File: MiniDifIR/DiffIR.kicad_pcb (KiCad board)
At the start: 2 copper layers, 33 x 24.8 mm, 17 parts, among them IC1 ATTINY25-SS, P1 AVR_ISP, P2 OUT

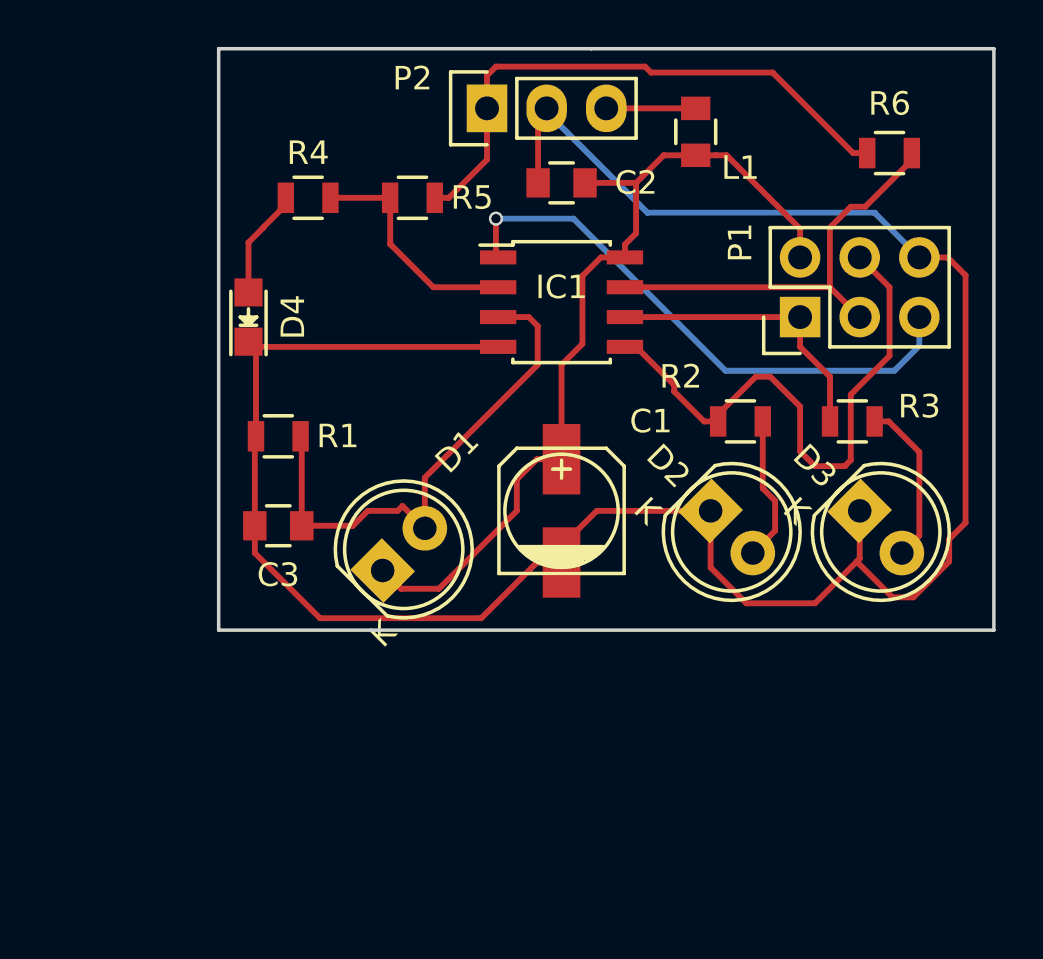
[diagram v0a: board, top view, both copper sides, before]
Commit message: thickened traces
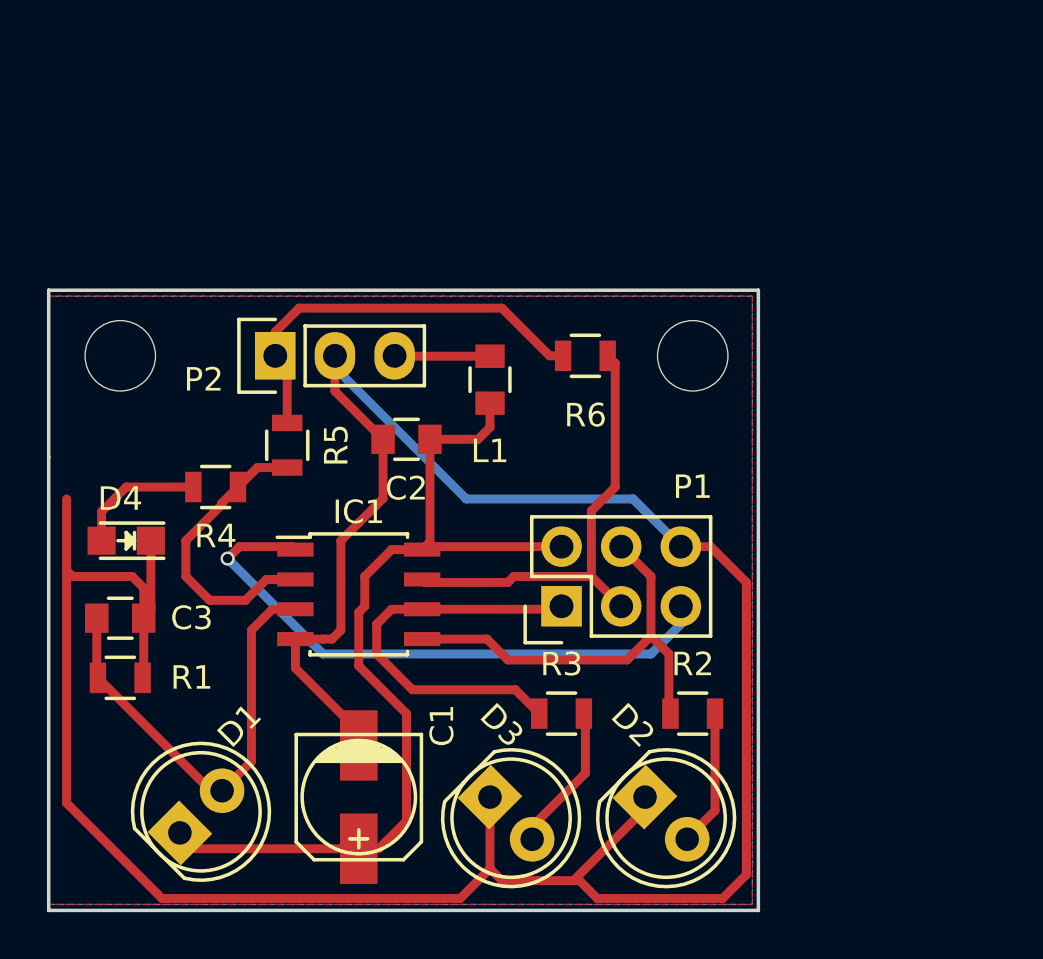
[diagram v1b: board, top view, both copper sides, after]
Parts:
- added W1: TEST_1P, Mounting_Holes:MountingHole_3mm, F.Cu at (126.0, 97.5)
- added W2: TEST_1P, Mounting_Holes:MountingHole_3mm, F.Cu at (150.4, 97.5)
- moved D3 19.9 mm to (141.7, 116.3)
- moved R3 17.6 mm to (144.8, 112.8)
- moved P1 16.0 mm to (144.8, 108.2)
- moved R6 15.6 mm to (145.8, 97.5)
- moved IC1 15.1 mm to (136.1, 107.7)
- moved C1 14.9 mm to (136.1, 116.3), turned to 270 degrees
- moved D1 14.1 mm to (128.5, 117.9)
- moved P2 13.9 mm to (132.6, 97.5)
- moved L1 13.7 mm to (141.7, 98.6)
- moved R4 12.9 mm to (130.0, 103.1)
- moved C2 12.8 mm to (138.2, 101.1)
- moved R2 12.6 mm to (150.4, 112.8)
- moved D2 12.5 mm to (148.3, 116.3)
- moved R1 12.3 mm to (126.0, 111.3), turned to 0 degrees
- moved R5 11.8 mm to (133.1, 101.3), turned to 270 degrees
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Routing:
- net GND: track 96.9 -> 119.4 mm
- net Net-(P2-Pad1): track 24.4 -> 17.6 mm
- net Net-(IC1-Pad5): track 24.7 -> 18.8 mm
- net Net-(IC1-Pad6): track 12.4 -> 17.4 mm
- net VCC: track 22.3 -> 19.4 mm
- net Net-(IC1-Pad2): track 9.88 -> 12.6 mm
- net Net-(C1-Pad1): track 36.9 -> 39.3 mm
- net Net-(IC1-Pad1): track 24.1 -> 25.4 mm
- net Net-(IC1-Pad7): track 18.0 -> 19.1 mm
- net Net-(D4-Pad2): track 4.69 -> 5.58 mm
- net Net-(D3-Pad2): track 7.05 -> 6.32 mm
- added copper zone on B.Cu, net Net-(IC1-Pad1)
- removed copper zone on B.Cu, net GND
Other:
- board size 33 x 24.8 mm -> 30.2 x 26.4 mm

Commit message: hex
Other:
- board text added: "+5"
- board text added: "GND"
- board text added: "SIG"
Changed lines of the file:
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@@
     (links 32)
     (no_connects 0)
-    (area 122.593499 92.4105 154.69138 121.233001)
+    (area 122.860999 94.666999 153.237001 121.233001)
     (thickness 1.6)
-    (drawings 5)
+    (drawings 8)
     (tracks 133)
     (zones 0)
@@
   )
   (setup
-    (last_trace_width 0.381)
+    (last_trace_width 0.25)
     (user_trace_width 0.381)
     (user_trace_width 0.508)
@@
     (visible_elements FFFFFF7F)
     (pcbplotparams
-      (layerselection 0x00030_80000001)
-      (usegerberextensions false)
+      (layerselection 0x010ff_80000001)
+      (usegerberextensions true)
       (excludeedgelayer true)
       (linewidth 0.100000)
@@
       (outputformat 1)
       (mirror false)
-      (drillshape 1)
+      (drillshape 0)
       (scaleselection 1)
-      (outputdirectory ""))
+      (outputdirectory gerbers/))
   )
   (net 0 "")
@@
       (net 15 "Net-(W2-Pad1)"))
   )
+  (gr_text SIG (at 129.286 97.536) (layer B.SilkS)
+    (effects (font (size 1.5 1.5) (thickness 0.3)))
+  )
+  (gr_text +5 (at 140.97 97.536) (layer B.SilkS)
+    (effects (font (size 1.5 1.5) (thickness 0.3)))
+  )
+  (gr_text GND (at 135.128 100.33) (layer B.SilkS)
+    (effects (font (size 1.5 1.5) (thickness 0.3)))
+  )
   (gr_line (start 122.936 94.742) (end 122.936 101.854) (angle 90) (layer Edge.Cuts) (width 0.15))
   (gr_line (start 153.162 94.742) (end 122.936 94.742) (angle 90) (layer Edge.Cuts) (width 0.15))
@@
   (segment (start 136.144 118.53164) (end 129.19964 118.53164) (width 0.381) (layer F.Cu) (net 1))
   (segment (start 129.19964 118.53164) (end 128.524 117.856) (width 0.381) (layer F.Cu) (net 1))
-  (segment (start 135.128 97.536) (end 135.128 98.044) (width 0.381) (layer B.Cu) (net 2) (status C00000))
-  (segment (start 135.128 98.044) (end 140.716 103.632) (width 0.381) (layer B.Cu) (net 2) (status 400000))
-  (segment (start 147.828 103.632) (end 149.86 105.664) (width 0.381) (layer B.Cu) (net 2) (status 800000))
+  (segment (start 135.128 97.536) (end 135.128 98.044) (width 0.381) (layer B.Cu) (net 2))
+  (segment (start 135.128 98.044) (end 140.716 103.632) (width 0.381) (layer B.Cu) (net 2))
+  (segment (start 147.828 103.632) (end 149.86 105.664) (width 0.381) (layer B.Cu) (net 2))
   (segment (start 140.716 103.632) (end 147.828 103.632) (width 0.381) (layer B.Cu) (net 2))
   (segment (start 145.288 119.888) (end 145.542 119.888) (width 0.381) (layer F.Cu) (net 2))
